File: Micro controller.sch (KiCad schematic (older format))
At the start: 1 part

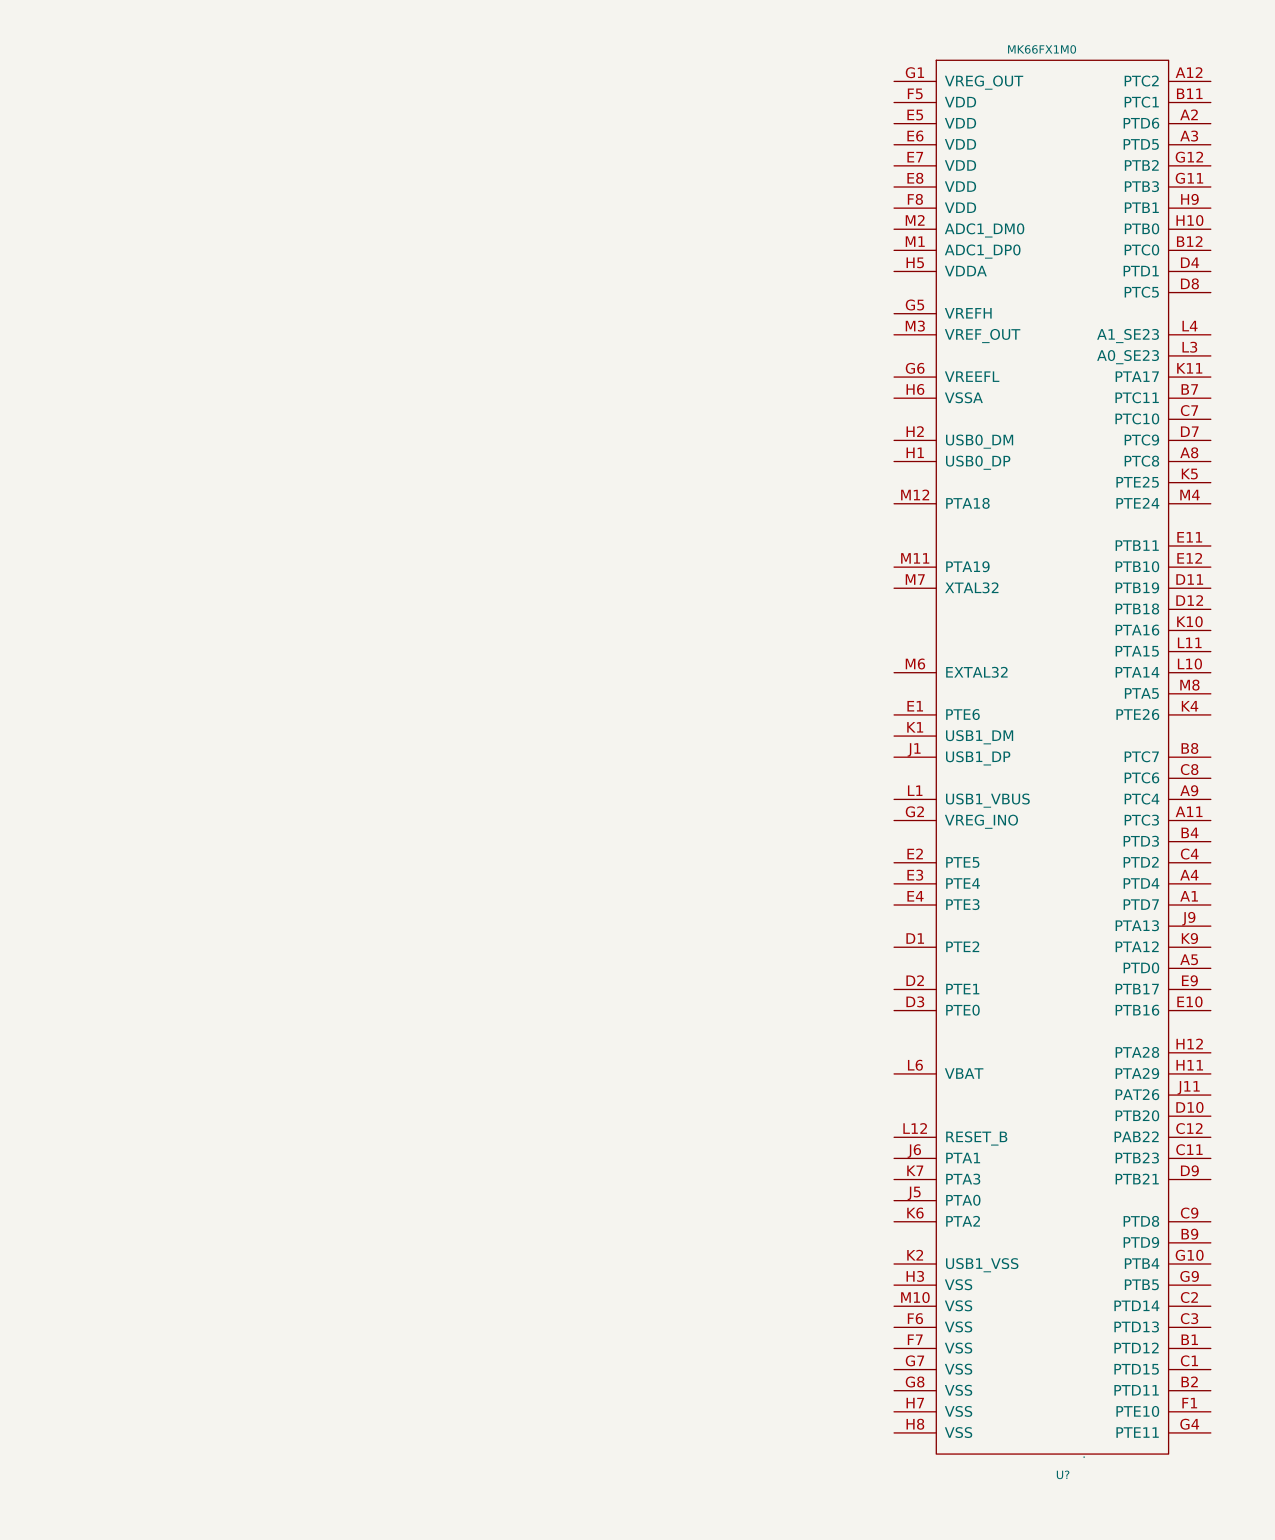
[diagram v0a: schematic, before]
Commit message: started wiring up the teensy schematic
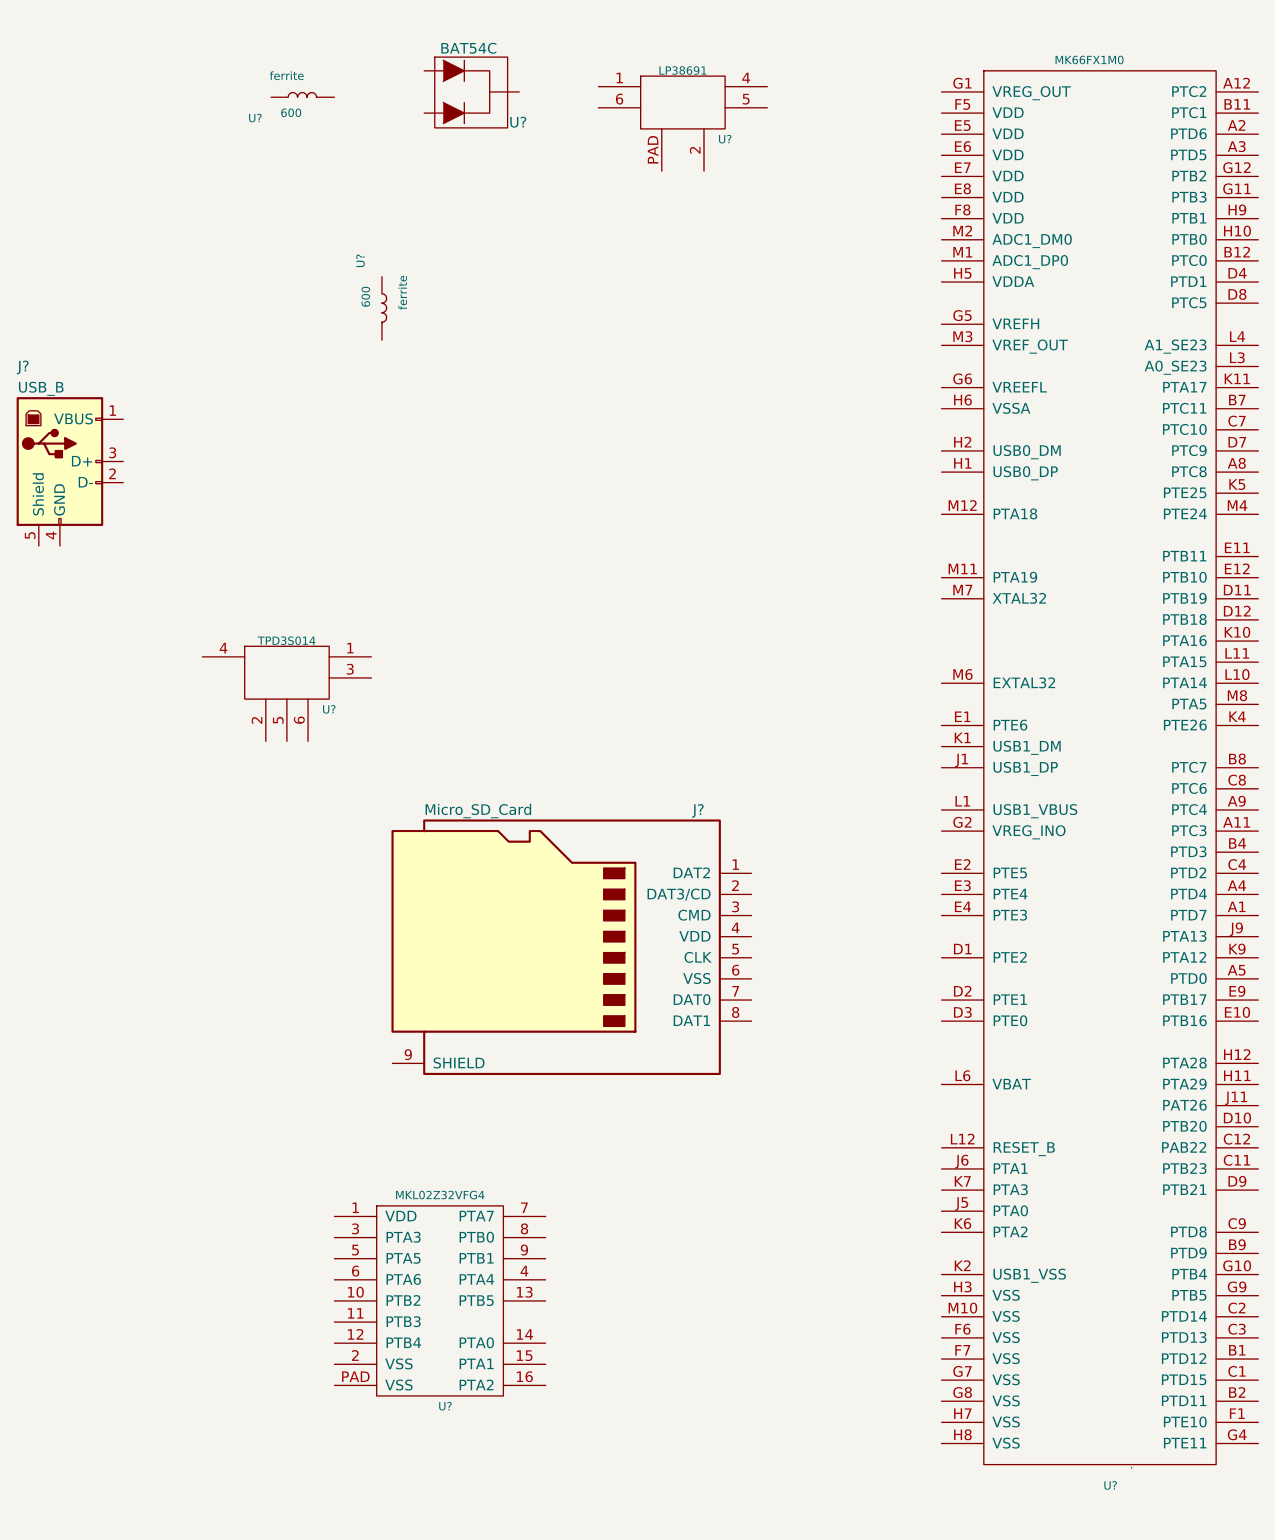
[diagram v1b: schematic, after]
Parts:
- added J?: Micro_SD_Card, symbol Micro_SD_Card
- added J?: USB_B, symbol USB_B
- added U?: LP38691, symbol LP38691
- added U?: BAT54C, PJC-Sandbox:SOT23-3P95_240X120L20X48N, symbol BAT54C
- added U? (x2): ferrite, symbol ferrite
- added U?: MKL02Z32VFG4, symbol MKL02Z32VFG4
- added U?: TPD3S014, symbol TPD3S014
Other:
- moved on the sheet: U?
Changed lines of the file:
@@
 LIBS:valves
 LIBS:Micromouse
-LIBS:teensy
+LIBS:1_PJC-Sandbox
+LIBS:Micromouse1.2-cache
 EELAYER 25 0
 EELAYER END
@@
 L MK66FX1M0 U?
 U 1 1 5946B40E
-P 5750 3775
-F 0 "U?" H 5750 175 39  0000 C CNN
-F 1 "MK66FX1M0" H 5650 6925 39  0000 C CNN
-F 2 "" H 5550 3775 39  0001 C CNN
-F 3 "" H 5550 3775 39  0001 C CNN
-F 4 "." H 5850 275 39  0000 C CNN "manf#"
-	1    5750 3775
+P 5975 3825
+F 0 "U?" H 5975 225 39  0000 C CNN
+F 1 "MK66FX1M0" H 5875 6975 39  0000 C CNN
+F 2 "" H 5775 3825 39  0001 C CNN
+F 3 "" H 5775 3825 39  0001 C CNN
+F 4 "." H 6075 325 39  0000 C CNN "manf#"
+	1    5975 3825
 	1    0    0    -1
 $EndComp
+$Comp
+L LP38691 U?
+U 1 1 59498B55
+P 3950 900
+F 0 "U?" H 4150 750 39  0000 C CNN
+F 1 "LP38691" H 3950 1075 39  0000 C CNN
+F 2 "" H 3850 800 39  0001 C CNN
+F 3 "" H 3850 800 39  0001 C CNN
+	1    3950 900
+	1    0    0    -1
+$EndComp
+$Comp
+L BAT54C U?
+U 1 1 59498B94
+P 2875 725
+F 0 "U?" H 3170 480 50  0000 C CNN
+F 1 "BAT54C" H 2935 830 50  0000 C CNN
+F 2 "PJC-Sandbox:SOT23-3P95_240X120L20X48N" H 2955 275 50  0001 C CNN
+F 3 "" H 2875 825 50  0000 C CNN
+F 4 "BAT54C" H 2945 385 60  0001 C CNN "manf#"
+	1    2875 725
+	1    0    0    -1
+$EndComp
+$Comp
+L ferrite U?
+U 1 1 59498BC8
+P 2100 850
+F 0 "U?" H 1925 750 39  0000 C CNN
+F 1 "ferrite" H 2075 950 39  0000 C CNN
+F 2 "" H 2100 850 39  0001 C CNN
+F 3 "" H 2095 760 39  0001 C CNN
+F 4 "600" H 2095 775 39  0000 C CNN "value"
+	1    2100 850
+	1    0    0    -1
+$EndComp
+$Comp
+L ferrite U?
+U 1 1 59498C30
+P 2525 1800
+F 0 "U?" H 2350 1700 39  0000 C CNN
+F 1 "ferrite" H 2500 1900 39  0000 C CNN
+F 2 "" H 2525 1800 39  0001 C CNN
+F 3 "" H 2520 1710 39  0001 C CNN
+F 4 "600" H 2520 1725 39  0000 C CNN "value"
+	1    2525 1800
+	0    1    1    0
+$EndComp
+$Comp
+L Micro_SD_Card J?
+U 1 1 59498C8F
+P 3375 4825
+F 0 "J?" H 2725 5425 50  0000 C CNN
+F 1 "Micro_SD_Card" H 4025 5425 50  0000 R CNN
+F 2 "" H 4525 5125 50  0001 C CNN
+F 3 "" H 3375 4825 50  0001 C CNN
+	1    3375 4825
+	-1   0    0    -1
+$EndComp
+$Comp
+L MKL02Z32VFG4 U?
+U 1 1 59498D14
+P 2800 6550
+F 0 "U?" H 2825 6050 39  0000 C CNN
+F 1 "MKL02Z32VFG4" H 2800 7050 39  0000 C CNN
+F 2 "" H 2800 6250 39  0001 C CNN
+F 3 "" H 2800 6250 39  0001 C CNN
+	1    2800 6550
+	1    0    0    -1
+$EndComp
+$Comp
+L TPD3S014 U?
+U 1 1 59498E84
+P 1975 3700
+F 0 "U?" H 2275 3650 39  0000 C CNN
+F 1 "TPD3S014" H 2075 3975 39  0000 C CNN
+F 2 "" H 1975 3700 39  0001 C CNN
+F 3 "" H 1975 3700 39  0001 C CNN
+	1    1975 3700
+	1    0    0    -1
+$EndComp
+$Comp
+L USB_B J?
+U 1 1 59498F09
+P 1000 2575
+F 0 "J?" H 800 3025 50  0000 L CNN
+F 1 "USB_B" H 800 2925 50  0000 L CNN
+F 2 "" H 1150 2525 50  0001 C CNN
+F 3 "" H 1150 2525 50  0001 C CNN
+	1    1000 2575
+	1    0    0    -1
+$EndComp

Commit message: finished the microcontroller connection
Finished the microcontrollers wiring up with out the pins.
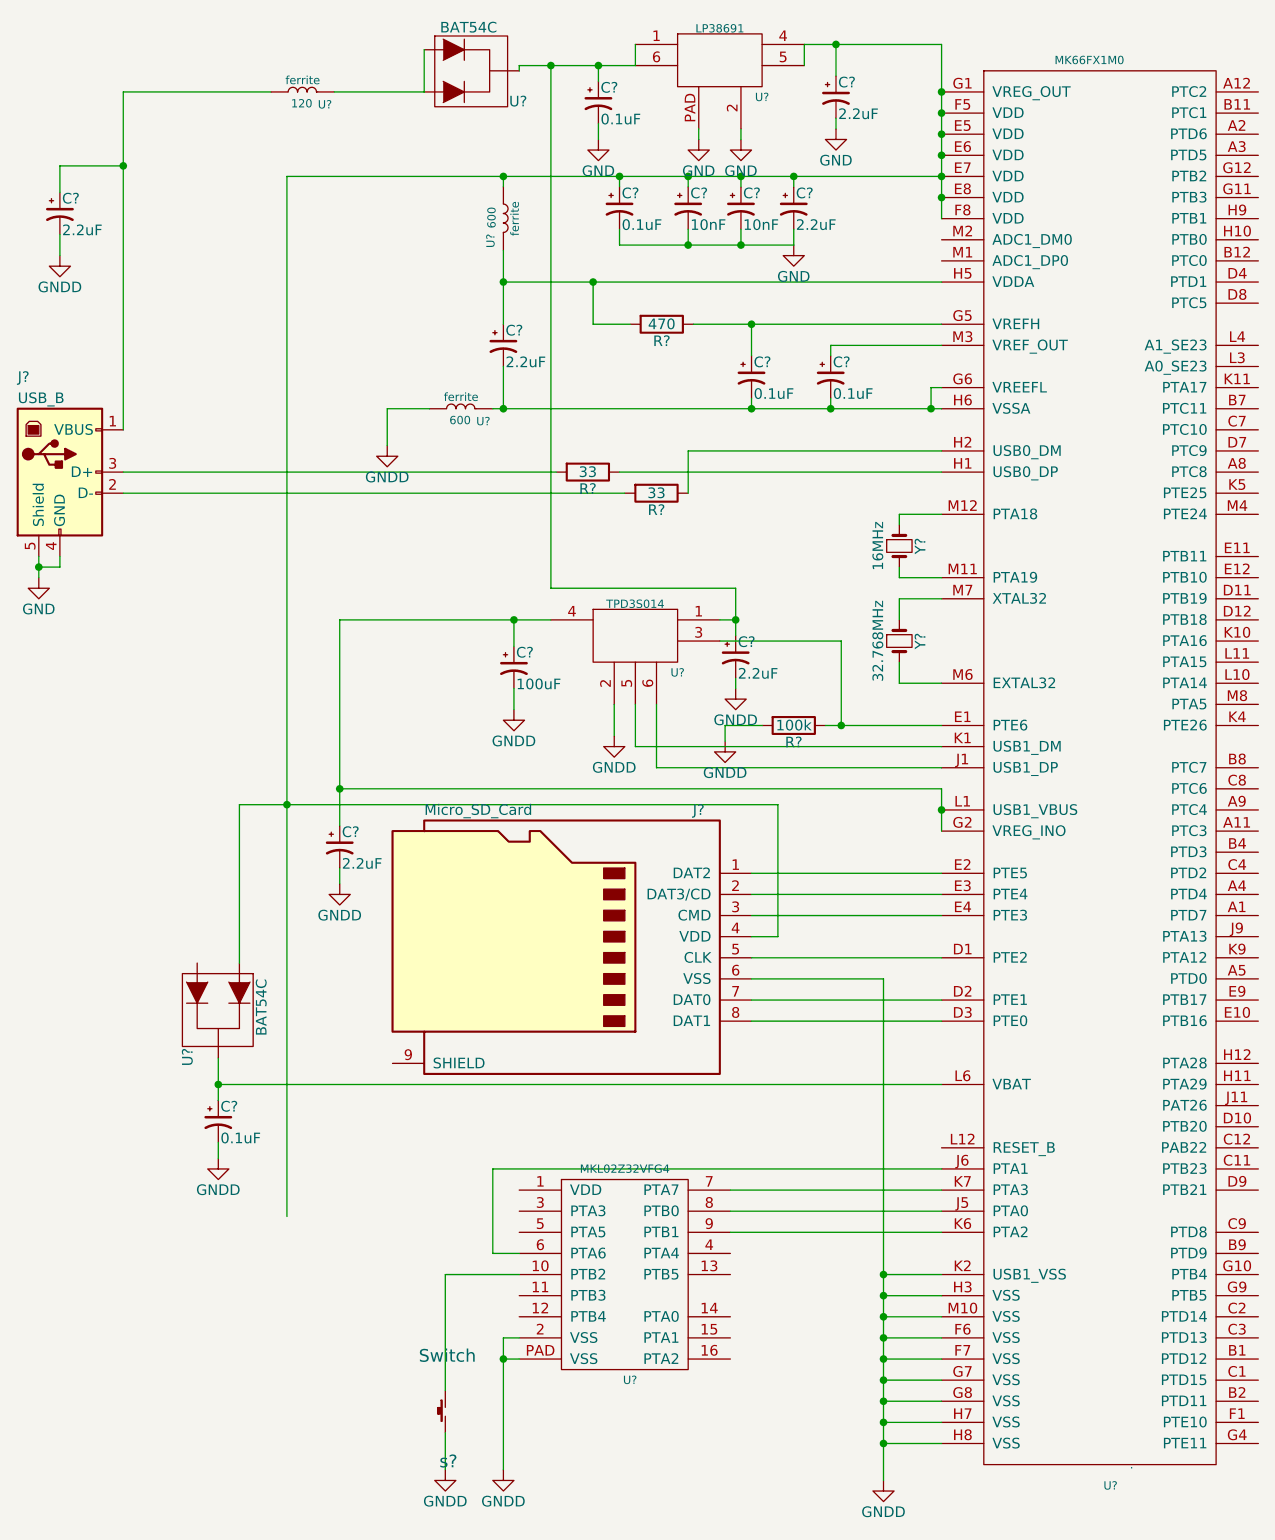
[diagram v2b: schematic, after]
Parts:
- removed U? (x2): ferrite, symbol ferrite
- added C? (x6): 2.2uF, symbol CP1_Small
- added C? (x5): 0.1uF, symbol CP1_Small
- added C? (x2): 10nF, symbol CP1_Small
- added C?: 100uF, symbol CP1_Small
- added R? (x2): 33, symbol R
- added R?: 470, symbol R
- added R?: 100k, symbol R
- added U? (x3): ferrite, symbol ferrite
- added U?: BAT54C, PJC-Sandbox:SOT23-3P95_240X120L20X48N, symbol BAT54C
- added Y?: 16MHz, symbol Crystal_Small
- added Y?: 32.768MHz, symbol Crystal_Small
- added s?: Switch, symbol Switch
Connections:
- net at U?.D1 (PTE2): now also J?.5 (CLK)
- net at U?.D2 (PTE1): now also J?.7 (DAT0)
- net at U?.D3 (PTE0): now also J?.8 (DAT1)
- net at U?.E1 (PTE6): now also U?.3, R?.1
- net at U?.E2 (PTE5): now also J?.1 (DAT2)
- net at U?.E3 (PTE4): now also J?.2 (DAT3/CD)
- net at U?.E4 (PTE3): now also J?.3 (CMD)
- net at U?.E5 (VDD): now also J?.4 (VDD), U?.4, U?.5, U?.E6 (VDD), U?.E7 (VDD), U?.E8 (VDD), U?.F5 (VDD), U?.F8 (VDD), U?.G1 (VREG_OUT), C?.1, C?.1, C?.1, C?.1, C?.1, U?.1, U?.1 (A)
- net GNDD: now reaches U?.F6 (VSS)
- net GNDD: now also J?.6 (VSS), U?.2, U?.2 (VSS), U?.F7 (VSS), U?.G7 (VSS), U?.G8 (VSS), U?.H3 (VSS), U?.H7 (VSS), U?.H8 (VSS), U?.K2 (USB1_VSS), U?.M10 (VSS), U?.PAD (VSS), C?.2, C?.2, C?.2, C?.2, C?.2, R?.2, U?.1, s?.2
- net at U?.G2 (VREG_INO): now also U?.4, U?.L1 (USB1_VBUS), C?.1, C?.1
- net at U?.G5 (VREFH): now also C?.1, R?.1
- net at U?.G6 (VREEFL): now also U?.H6 (VSSA), C?.2, C?.2, C?.2, U?.2
- net at U?.H1 (USB0_DP): now also R?.1
- net at U?.H2 (USB0_DM): now also R?.1
- net at U?.H5 (VDDA): now also C?.1, R?.2, U?.2
- net at U?.J1 (USB1_DP): now also U?.6
- net at U?.J5 (PTA0): now also U?.8 (PTB0)
- net at U?.J6 (PTA1): now also U?.6 (PTA6)
- net at U?.K1 (USB1_DM): now also U?.5
- net at U?.K6 (PTA2): now also U?.9 (PTB1)
- net at U?.K7 (PTA3): now also U?.7 (PTA7)
- net at U?.L6 (VBAT): now also C?.1, U?.3
- net at U?.M11 (PTA19): now also Y?.2
- net at U?.M12 (PTA18): now also Y?.1
- net at U?.M3 (VREF_OUT): now also C?.1
- net at U?.M6 (EXTAL32): now also Y?.2
- net at U?.M7 (XTAL32): now also Y?.1
- net at U?.1: now also U?.1, U?.3, U?.6, C?.1, C?.1
- net GND: now reaches U?.2
- net GND: now also J?.4 (GND), J?.5 (Shield), U?.PAD, C?.2, C?.2, C?.2, C?.2, C?.2, C?.2
- net at U?.1 (A): now also U?.2 (A), U?.2
- net at U?.10 (PTB2): now also s?.1
- net at J?.1 (VBUS): now also C?.1, U?.1
- net at J?.2 (D-): now also R?.2
- net at J?.3 (D+): now also R?.2
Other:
- moved on the sheet: J?, U?
